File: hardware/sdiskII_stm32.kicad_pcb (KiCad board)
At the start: 2 copper layers, 105 x 59 mm, 34 parts, among them J2 APPLE_SDISKII, U1 74LS123, U2 MicroSD_SPI_CD, U3 74LS125, U4 74LS14, U5 74LS74, U6 74LS393, U7 74LS86, U8 DM-OLED096-636, U9 TLV76133DCY

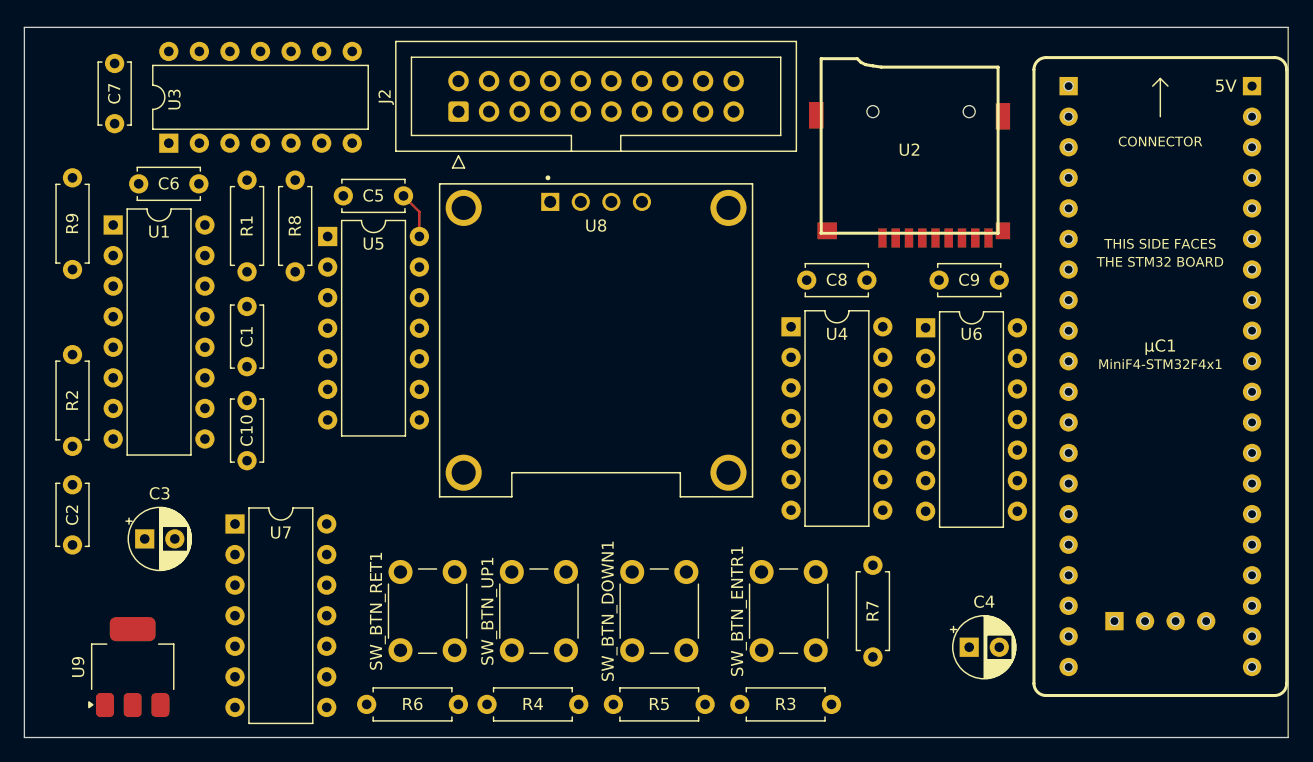
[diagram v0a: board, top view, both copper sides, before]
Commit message: all images working
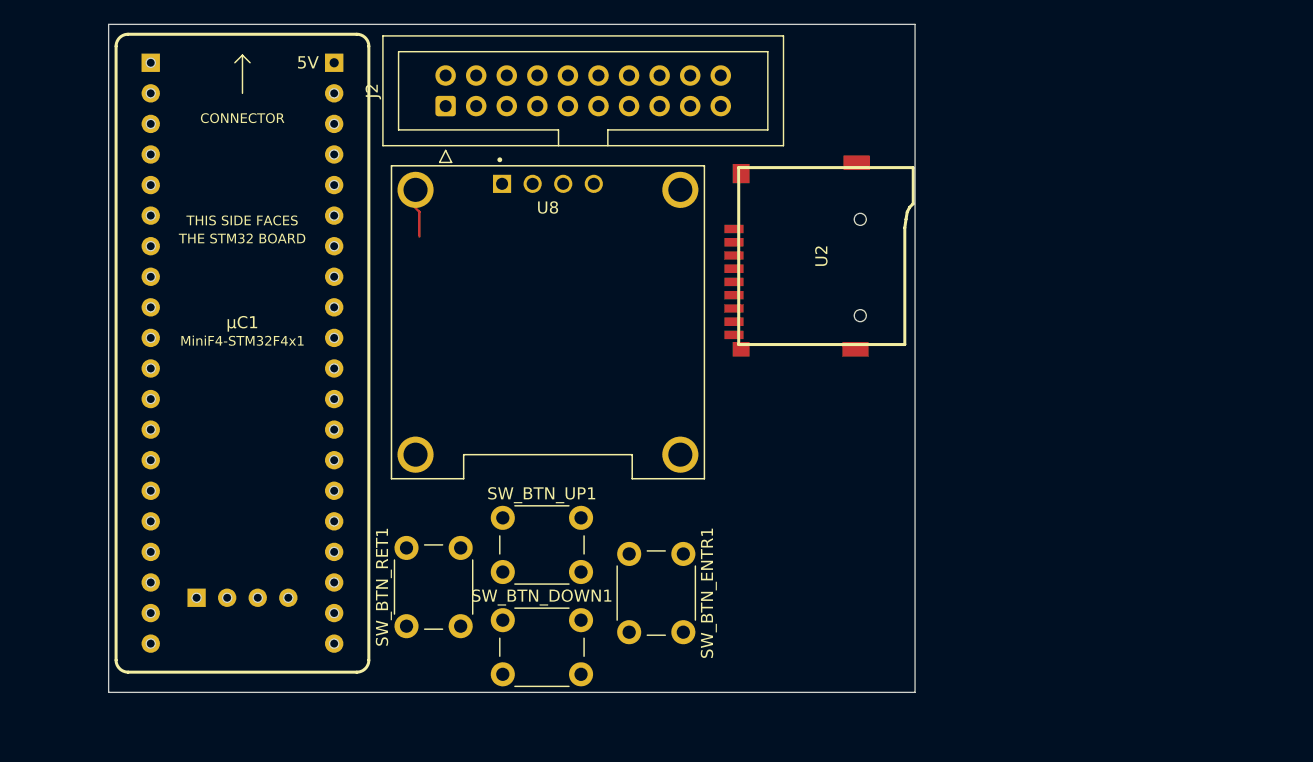
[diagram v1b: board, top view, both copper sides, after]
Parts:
- removed C1: 220pF, Capacitor_THT:C_Disc_D5.0mm_W2.5mm_P5.00mm
- removed C10, C5, C6, C7, C8, C9: 100nF, Capacitor_THT:C_Disc_D5.0mm_W2.5mm_P5.00mm
- removed C2: 47pF, Capacitor_THT:C_Disc_D5.0mm_W2.5mm_P5.00mm
- removed C3: 10uF, Capacitor_THT:CP_Radial_D5.0mm_P2.50mm
- removed C4: 10uF 25V, Capacitor_THT:CP_Radial_D5.0mm_P2.50mm
- removed R1, R2, R3, R4, R5, R6: 10k, Resistor_THT:R_Axial_DIN0207_L6.3mm_D2.5mm_P7.62mm_Horizontal
- removed R7, R8, R9: 1k, Resistor_THT:R_Axial_DIN0207_L6.3mm_D2.5mm_P7.62mm_Horizontal
- removed U1: 74LS123, Package_DIP:DIP-16_W7.62mm
- removed U3: 74LS125, Package_DIP:DIP-14_W7.62mm
- removed U4: 74LS14, Package_DIP:DIP-14_W7.62mm
- removed U5: 74LS74, Package_DIP:DIP-14_W7.62mm
- removed U6: 74LS393, Package_DIP:DIP-14_W7.62mm
- removed U7: 74LS86, Package_DIP:DIP-14_W7.62mm
- removed U9: TLV76133DCY, Package_TO_SOT_SMD:SOT-223-3_TabPin2
- U2: value MicroSD_SPI_CD -> MicroSD_SDIO
- moved μC1 76.3 mm to (99.1, 46.6)
- moved U2 15.4 mm to (139.2, 38.5), turned to -90 degrees
- moved SW_BTN_DOWN1 11.0 mm to (120.8, 68.8), turned to 0 degrees
- moved SW_BTN_UP1 11.0 mm to (120.8, 60.2), turned to 0 degrees
- moved SW_BTN_ENTR1 10.3 mm to (135.8, 63.2), turned to -90 degrees
- moved U8 4.27 mm to (124.5, 44.0)
- moved SW_BTN_RET1 2.06 mm to (112.8, 69.2)
- moved J2 1.16 mm to (116.0, 26.0)
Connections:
- J2 pad 16: RDDATA -> RD_DATA
- J2 pad 18: WRDATA -> WR_DATA
- SW_BTN_DOWN1 pad 1: Net-(R5-Pad1) -> +3.3V
- SW_BTN_ENTR1 pad 1: Net-(R3-Pad1) -> +3.3V
- SW_BTN_RET1 pad 1: Net-(R6-Pad1) -> +3.3V
- SW_BTN_UP1 pad 1: Net-(R4-Pad1) -> +3.3V
- U2 pad 1: (no net) -> SDIO_D2
- U2 pad 2: SPI2_NSS -> SDIO_D3
- U2 pad 3: SPI2_MOSI -> SDIO_CMD
- U2 pad 5: SPI2_SCK -> SDIO_CK
- U2 pad 7: SPI2_MISO -> SDIO_DO
- U2 pad 8: (no net) -> SDIO_D1
- μC1 pad 1: SPI2_NSS -> unconnected-(μC1-B12-Pad1)
- μC1 pad 10: unconnected-(μC1-A15-Pad10) -> USART1_TX
- μC1 pad 11: SPI3_SCK -> USART1_RX
- μC1 pad 12: SPI1_SCK -> SDIO_DO
- μC1 pad 13: NEW_WRDATA -> SDIO_D3
- μC1 pad 16: TIM4 -> unconnected-(μC1-B8-Pad16)
- μC1 pad 2: SPI2_SCK -> unconnected-(μC1-B13-Pad2)
- μC1 pad 3: SPI2_MISO -> DEBUG
- μC1 pad 30: /DRIVE_ENABLE -> /DEVICE_ENABLE
- μC1 pad 32: SP1_MISO -> SDIO_CMD
- μC1 pad 33: SD_EJECT -> WR_DATA
- μC1 pad 34: unconnected-(μC1-B0-Pad34) -> RD_DATA
- μC1 pad 35: WRPROT -> TIM3_CH4
- μC1 pad 36: unconnected-(μC1-B2-Pad36) -> WR_PROTECT
- μC1 pad 37: BTN_RET -> SD_EJECT
- μC1 pad 4: SPI2_MOSI -> SDIO_CK
- μC1 pad 5: unconnected-(μC1-A8-Pad5) -> SDIO_D1
- μC1 pad 6: USART1_TX -> SDIO_D2
- μC1 pad 7: USART1_RX -> TIM1_CH3
- μC1 pad 8: unconnected-(μC1-A11-Pad8) -> BTN_RET
- μC1 pad 9: unconnected-(μC1-A12-Pad9) -> WR_DATA
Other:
- board size 105 x 59 mm -> 67 x 55.5 mm

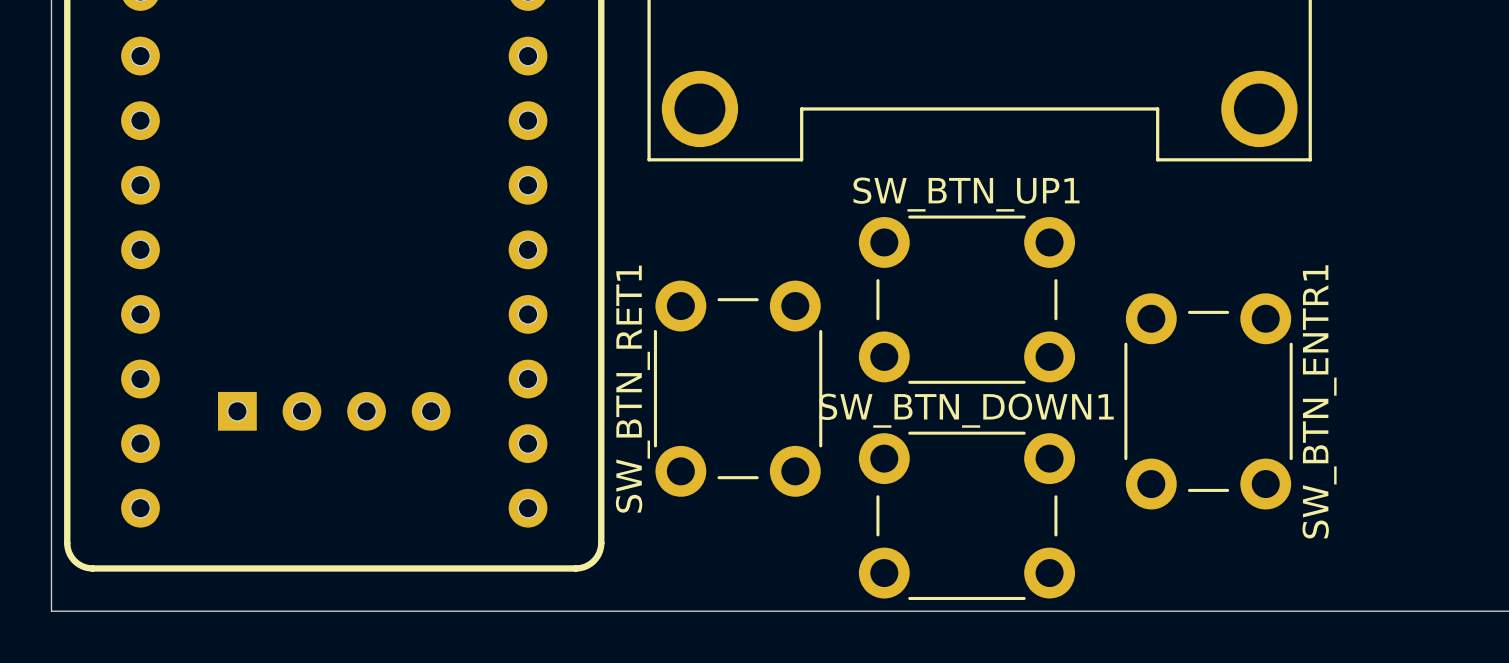
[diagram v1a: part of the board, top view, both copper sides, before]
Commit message: Code cleaning, warning suppress, casting
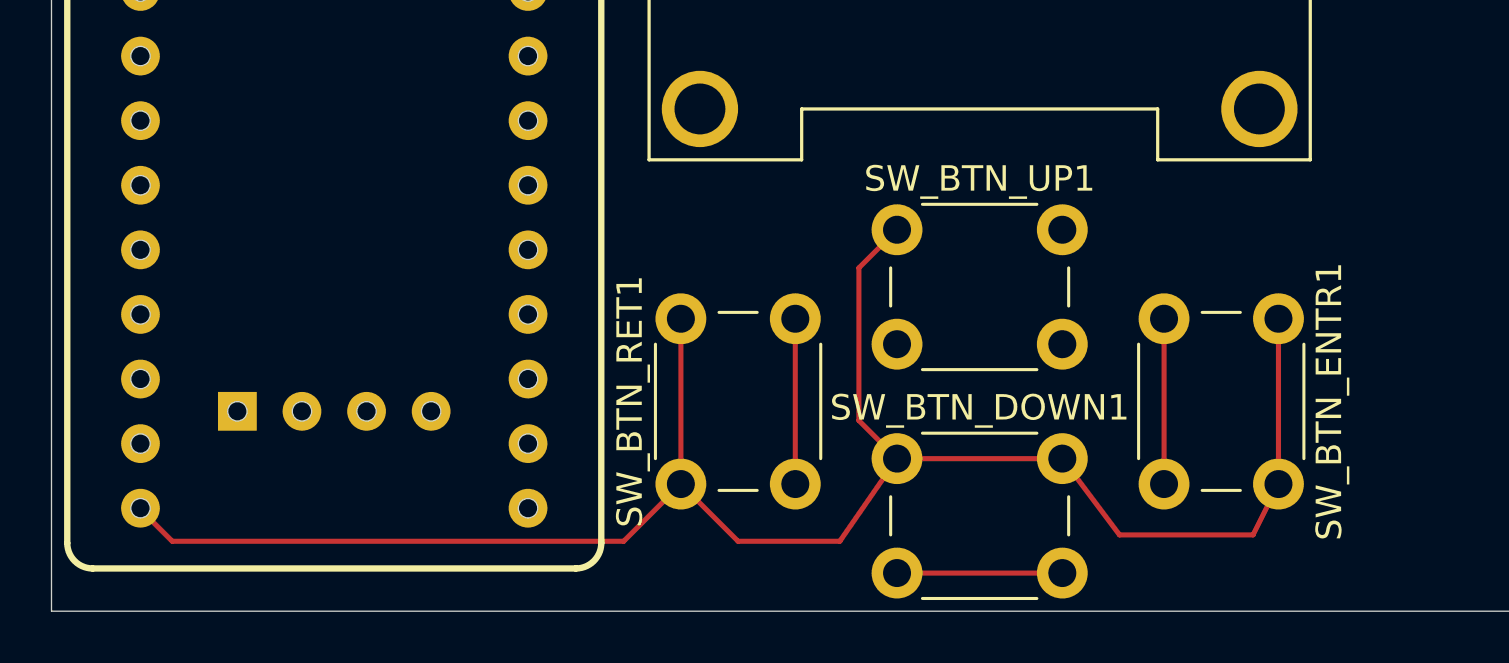
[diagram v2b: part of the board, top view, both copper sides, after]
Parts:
- moved SW_BTN_UP1 0.71 mm to (121.2, 59.8)
- moved SW_BTN_DOWN1 0.50 mm to (121.2, 68.8)
- moved SW_BTN_ENTR1 0.50 mm to (136.2, 63.2)
- moved SW_BTN_RET1 0.50 mm to (112.8, 69.8)
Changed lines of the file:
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@@
 		(tags "Through hole vertical IDC box header THT 2x10 2.54mm double row")
 		(property "Reference" "J2"
-			(at 1.27 -6.1 270)
+			(at 1.27 -6.1 -90)
 			(layer "F.SilkS")
 			(effects
@@
 		)
 		(property "Value" "APPLE_SDISKII"
-			(at 1.27 28.96 270)
+			(at 1.27 28.96 -90)
 			(layer "F.Fab")
 			(effects
@@
 		)
 		(fp_text user "${REFERENCE}"
-			(at 1.27 11.43 360)
+			(at 1.27 11.43 0)
 			(layer "F.Fab")
 			(effects
@@
 	(footprint "Button_Switch_THT:SW_PUSH_6mm"
 		(layer "F.Cu")
-		(at 120.75 60.25)
+		(at 121.25 59.75)
 		(descr "Generic 6mm SW tactile push button")
 		(tags "tact sw push 6mm")
 		(property "Reference" "SW_BTN_UP1"
-			(at 3.25 -2 360)
+			(at 3.25 -2 0)
 			(layer "F.SilkS")
 			(effects
@@
 		)
 		(property "Value" "SW_Push"
-			(at 3.75 6.7 360)
+			(at 3.75 6.7 0)
 			(layer "F.Fab")
 			(effects
@@
 		)
 		(fp_text user "${REFERENCE}"
-			(at 3.25 2.25 360)
+			(at 3.25 2.25 0)
 			(layer "F.Fab")
 			(effects
@@
 	(footprint "Button_Switch_THT:SW_PUSH_6mm"
 		(layer "F.Cu")
-		(at 135.75 63.25 -90)
+		(at 136.25 63.25 -90)
 		(descr "Generic 6mm SW tactile push button")
 		(tags "tact sw push 6mm")
@@
 	(footprint "Button_Switch_THT:SW_PUSH_6mm"
 		(layer "F.Cu")
-		(at 112.75 69.25 90)
+		(at 112.75 69.75 90)
 		(descr "Generic 6mm SW tactile push button")
 		(tags "tact sw push 6mm")
@@
 	(footprint "Button_Switch_THT:SW_PUSH_6mm"
 		(layer "F.Cu")
-		(at 120.75 68.75)
+		(at 121.25 68.75)
 		(descr "Generic 6mm SW tactile push button")
 		(tags "tact sw push 6mm")
 		(property "Reference" "SW_BTN_DOWN1"
-			(at 3.25 -2 360)
+			(at 3.25 -2 0)
 			(layer "F.SilkS")
 			(effects
@@
 		)
 		(property "Value" "SW_Push"
-			(at 3.75 6.7 360)
+			(at 3.75 6.7 0)
 			(layer "F.Fab")
 			(effects
@@
 		)
 		(fp_text user "${REFERENCE}"
-			(at 3.25 2.25 360)
+			(at 3.25 2.25 0)
 			(layer "F.Fab")
 			(effects
@@
 		)
 	)
+	(gr_line
+		(start 136.25 63.25)
+		(end 136.25 69.75)
+		(stroke
+			(width 0.2)
+			(type default)
+		)
+		(layer "F.Cu")
+		(net 21)
+	)
+	(gr_line
+		(start 110.5 72)
+		(end 112.75 69.75)
+		(stroke
+			(width 0.2)
+			(type default)
+		)
+		(layer "F.Cu")
+		(net 21)
+	)
+	(gr_line
+		(start 127.75 73.25)
+		(end 121.25 73.25)
+		(stroke
+			(width 0.2)
+			(type default)
+		)
+		(layer "F.Cu")
+		(net 16)
+	)
+	(gr_line
+		(start 119.75 61.25)
+		(end 121.25 59.75)
+		(stroke
+			(width 0.2)
+			(type default)
+		)
+		(layer "F.Cu")
+		(net 21)
+	)
+	(gr_line
+		(start 115 72)
+		(end 119 72)
+		(stroke
+			(width 0.2)
+			(type default)
+		)
+		(layer "F.Cu")
+		(net 21)
+	)
+	(gr_line
+		(start 121.25 68.75)
+		(end 127.75 68.75)
+		(stroke
+			(width 0.2)
+			(type default)
+		)
+		(layer "F.Cu")
+		(net 21)
+	)
+	(gr_line
+		(start 117.25 63.25)
+		(end 117.25 69.75)
+		(stroke
+			(width 0.2)
+			(type default)
+		)
+		(layer "F.Cu")
+		(net 18)
+	)
+	(gr_line
+		(start 130 71.75)
+		(end 127.75 68.75)
+		(stroke
+			(width 0.2)
+			(type default)
+		)
+		(layer "F.Cu")
+		(net 21)
+	)
+	(gr_line
+		(start 112.75 69.75)
+		(end 115 72)
+		(stroke
+			(width 0.2)
+			(type default)
+		)
+		(layer "F.Cu")
+		(net 21)
+	)
+	(gr_line
+		(start 112.75 63.25)
+		(end 112.75 69.75)
+		(stroke
+			(width 0.2)
+			(type default)
+		)
+		(layer "F.Cu")
+		(net 21)
+	)
+	(gr_line
+		(start 119 72)
+		(end 121.25 68.75)
+		(stroke
+			(width 0.2)
+			(type default)
+		)
+		(layer "F.Cu")
+		(net 21)
+	)
+	(gr_line
+		(start 121.25 68.75)
+		(end 119.75 67.25)
+		(stroke
+			(width 0.2)
+			(type default)
+		)
+		(layer "F.Cu")
+		(net 21)
+	)
+	(gr_line
+		(start 135.25 71.75)
+		(end 130 71.75)
+		(stroke
+			(width 0.2)
+			(type default)
+		)
+		(layer "F.Cu")
+		(net 21)
+	)
+	(gr_line
+		(start 131.75 69.75)
+		(end 131.75 63.25)
+		(stroke
+			(width 0.2)
+			(type default)
+		)
+		(layer "F.Cu")
+		(net 17)
+	)
+	(gr_line
+		(start 119.75 67.25)
+		(end 119.75 61.25)
+		(stroke
+			(width 0.2)
+			(type default)
+		)
+		(layer "F.Cu")
+		(net 21)
+	)
+	(gr_line
+		(start 92.75 72)
+		(end 110.5 72)
+		(stroke
+			(width 0.2)
+			(type default)
+		)
+		(layer "F.Cu")
+		(net 21)
+	)
+	(gr_line
+		(start 136.25 69.75)
+		(end 135.25 71.75)
+		(stroke
+			(width 0.2)
+			(type default)
+		)
+		(layer "F.Cu")
+		(net 21)
+	)
+	(gr_line
+		(start 91.5 70.75)
+		(end 92.75 72)
+		(stroke
+			(width 0.2)
+			(type default)
+		)
+		(layer "F.Cu")
+		(net 21)
+	)
 	(gr_rect

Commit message: new realease with gerber
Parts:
- added  : LOGO, LOGO, F.Cu at (147.0, 121.7)
- added  : LOGO, LOGO, F.Cu at (138.6, 140.2)
- added J1: PWR, Connector_PinHeader_2.54mm:PinHeader_1x02_P2.54mm_Vertical, F.Cu at (204.8, 98.8)
- added J3: DBG, Connector_PinHeader_2.54mm:PinHeader_1x05_P2.54mm_Vertical, F.Cu at (204.9, 118.0)
- added J4: UART, Connector_PinHeader_2.54mm:PinHeader_1x03_P2.54mm_Vertical, F.Cu at (135.2, 105.0)
- added J5: TIM, Connector_PinHeader_2.54mm:PinHeader_1x03_P2.54mm_Vertical, F.Cu at (135.2, 116.7)
- added J6: STLINK, Connector_PinHeader_2.54mm:PinHeader_1x04_P2.54mm_Vertical, F.Cu at (135.2, 128.2)
- added R1: 1k, Resistor_THT:R_Axial_DIN0207_L6.3mm_D2.5mm_P10.16mm_Horizontal, F.Cu at (201.6, 127.3)
- added R2: 1k, Resistor_THT:R_Axial_DIN0207_L6.3mm_D2.5mm_P10.16mm_Horizontal, F.Cu at (201.6, 129.5)
- added R3: 1k, Resistor_THT:R_Axial_DIN0207_L6.3mm_D2.5mm_P10.16mm_Horizontal, F.Cu at (204.9, 121.1)
- U2: footprint sdisk_stm32:GCT-MEM2055-00-190-01-A -> sdisk_stm32:GCT-MEM2055-00-190-01-A_VIB
- μC1: footprint acheron_Hardware.pretty-master:Mini_F4X1_STM32 -> acheron_Hardware.pretty-master:Mini_F4X1_STM32_VIB
- moved UP1 99.0 mm to (190.0, 130.9), turned to 180 degrees
- moved U8 91.1 mm to (186.8, 110.5)
- moved ENTR1 91.1 mm to (198.5, 129.7)
- moved J2 91.1 mm to (178.3, 92.5)
- moved μC1 90.9 mm to (161.7, 112.6)
- moved DOWN1 90.9 mm to (183.5, 134.9)
- moved RET1 89.7 mm to (179.5, 129.7), turned to -90 degrees
- moved U2 63.2 mm to (141.4, 101.7), turned to 0 degrees
- renumbered SW_BTN_DOWN1 to DOWN1, SW_BTN_ENTR1 to ENTR1, SW_BTN_RET1 to RET1, SW_BTN_UP1 to UP1
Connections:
- J2 pad 14: DRIVE_ENABLE -> DEVICE_ENABLE
- U2 pad 10: (no net) -> GND
- U2 pad ~: (no net) -> GND
- μC1 pad 1: unconnected-(μC1-B12-Pad1) -> BTN_RET
- μC1 pad 18: unconnected-(μC1-5Vi-Pad18) -> PWR_IN
- μC1 pad 2: unconnected-(μC1-B13-Pad2) -> SD_EJECT
- μC1 pad 22: BTN_ENTR -> BTN_DOWN
- μC1 pad 24: BTN_DOWN -> BTN_ENTR
- μC1 pad 30: /DEVICE_ENABLE -> DEVICE_ENABLE
- μC1 pad 31: SP1_SCK -> WR_DATA
- μC1 pad 37: SD_EJECT -> TIM2_CH3
- μC1 pad 41: unconnected-(μC1-3.3V-Pad41) -> +3.3V
- μC1 pad 42: unconnected-(μC1-SDIO-Pad42) -> SDIO
- μC1 pad 43: unconnected-(μC1-SCK-Pad43) -> SCK
- μC1 pad 44: unconnected-(μC1-GND-Pad44) -> GND
- μC1 pad 7: TIM1_CH3 -> unconnected-(μC1-A10-Pad7)
- μC1 pad 8: BTN_RET -> unconnected-(μC1-A11-Pad8)
- μC1 pad 9: WR_DATA -> unconnected-(μC1-A12-Pad9)
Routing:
- net +3.3V: track 0.00 -> 208.6 mm
- net GND: track 0.00 -> 180.2 mm, vias 0 -> 2
- net WR_REQ: track 0.00 -> 144.3 mm, vias 0 -> 1
- net BTN_RET: track 0.00 -> 122.6 mm
- net PWR_IN: track 0.00 -> 105.4 mm
- net DEVICE_ENABLE: track 0.00 -> 103.3 mm
- net WR_DATA: track 0.00 -> 78.3 mm
- net WR_PROTECT: track 0.00 -> 74.7 mm, vias 0 -> 1
- net TIM2_CH3: track 0.00 -> 62.6 mm, vias 0 -> 1
- net RD_DATA: track 0.00 -> 62.5 mm
- net TIM3_CH4: track 0.00 -> 60.2 mm, vias 0 -> 1
- net VCC: track 3.92 -> 63.9 mm
- net I2C_SDA: track 0.00 -> 49.4 mm
- net DEBUG: track 0.00 -> 47.2 mm
- net I2C_SCL: track 0.00 -> 45.4 mm
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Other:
- board size 67 x 55.5 mm -> 76 x 56.3 mm
- board text added: "+3.3V"
- board text added: "Board Rev 1"
- board text added: "DE"
- board text added: "DEBUG"
- board text added: "GND"
- board text added: "PB14"
- board text added: "PWR"
- board text added: "RDD"
- board text added: "RX"
- board text added: "SCK"
- board text added: "SCL"
- board text added: "SDA"
- board text added: "SDIO"
- board text added: "STLINK"
- board text added: "STM32F411"
- board text added: "TIM2CH3"
- board text added: "TIM3CH4"
- board text added: "TX"
- board text added: "UART"
- board text added: "WRP"
- board text added: "WRQ"
- board text added: "vincent@besson.be"

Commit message: board rev20
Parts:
- J3: value DBG -> Conn_01x06; footprint Connector_PinHeader_2.54mm:PinHeader_1x05_P2.54mm_Vertical -> Connector_PinHeader_2.54mm:PinHeader_1x06_P2.54mm_Vertical
- J5: value TIM -> Conn_01x04; footprint Connector_PinHeader_2.54mm:PinHeader_1x03_P2.54mm_Vertical -> Connector_PinHeader_2.54mm:PinHeader_1x04_P2.54mm_Vertical
- moved J3 10.0 mm to (204.8, 108.0), turned to 0 degrees
- moved R3 2.55 mm to (204.9, 123.7)
- moved J5 0.29 mm to (135.0, 116.5)
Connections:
- U2 pad ~: GND -> (no net)
- μC1 pad 3: DEBUG -> TIM1_CH2N
- μC1 pad 7: unconnected-(μC1-A10-Pad7) -> DEBUG
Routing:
- net TIM1_CH2N: track 0.00 -> 47.2 mm
- net DEBUG: track 47.2 -> 0.00 mm
- net GND: track 180.2 -> 183.8 mm
- net VCC: track 63.9 -> 67.1 mm
- net DEVICE_ENABLE: track 103.3 -> 105.9 mm

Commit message: board rev2
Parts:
- added BZ1: Buzzer, buzzer:AS-1201B-LF, F.Cu at (143.8, 131.8)
- moved   6.20 mm to (147.0, 115.5)
- moved J3 0.29 mm to (204.8, 107.7)
- moved J6 0.24 mm to (135.0, 128.2)
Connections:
- J3 pad 1: WR_DATA -> RD_DATA
- J3 pad 2: WR_PROTECT -> WR_REQ
- J3 pad 4: WR_REQ -> WR_PROTECT
- J3 pad 5: RD_DATA -> WR_DATA
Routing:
- net DEBUG: track 0.00 -> 77.5 mm, vias 0 -> 2
- net GND: track 183.8 -> 232.5 mm, vias 2 -> 3
- net TIM1_CH2N: track 47.2 -> 64.5 mm
- net SDIO: track 27.0 -> 28.0 mm
- net SCK: track 29.6 -> 30.6 mm
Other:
- board text added: "Board Rev 2"
- board text added: "PA10"
- board text removed: "Board Rev 1"
- board text removed: "PB14"

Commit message: v0.74 - Not running
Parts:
- moved J1 0.16 mm to (205.0, 98.8)
- moved J3 0.16 mm to (205.0, 107.7)
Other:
- board text added: "3.3V"
- board text removed: "DEBUG"
